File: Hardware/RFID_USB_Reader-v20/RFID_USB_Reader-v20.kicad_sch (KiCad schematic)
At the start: 18 parts, among them J1 USB_C_Receptacle, J3 SMD_1x1mm, J5 Conn_01x08, Q1 MMBT2222A, U3 CH340C

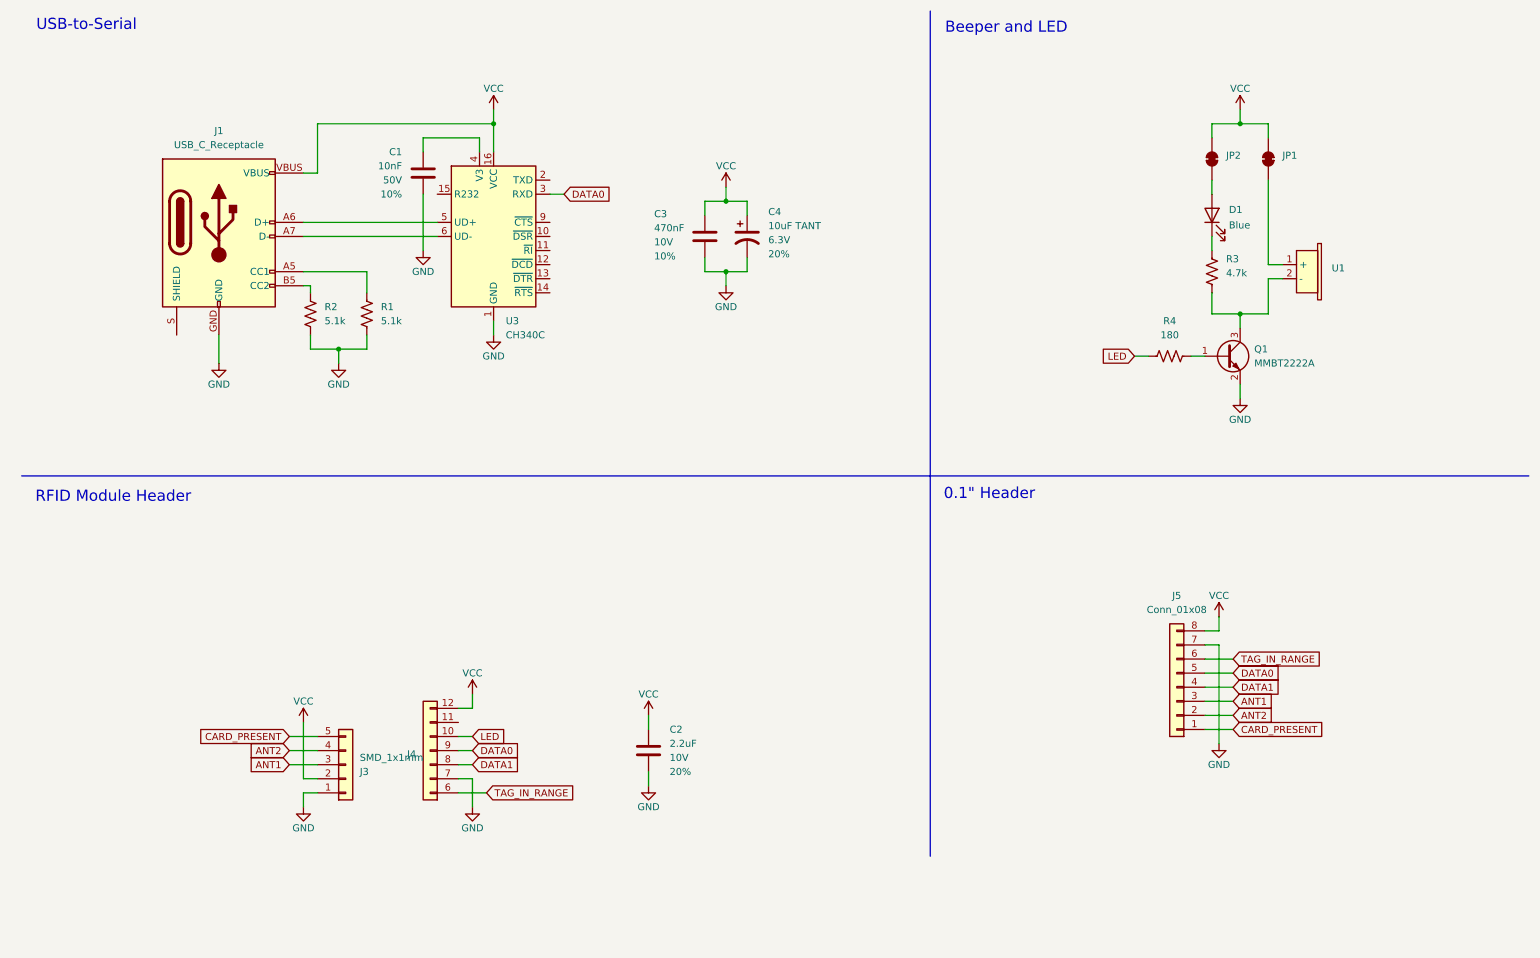
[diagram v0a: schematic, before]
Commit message: Update to small symbols. Add RFID outline device.
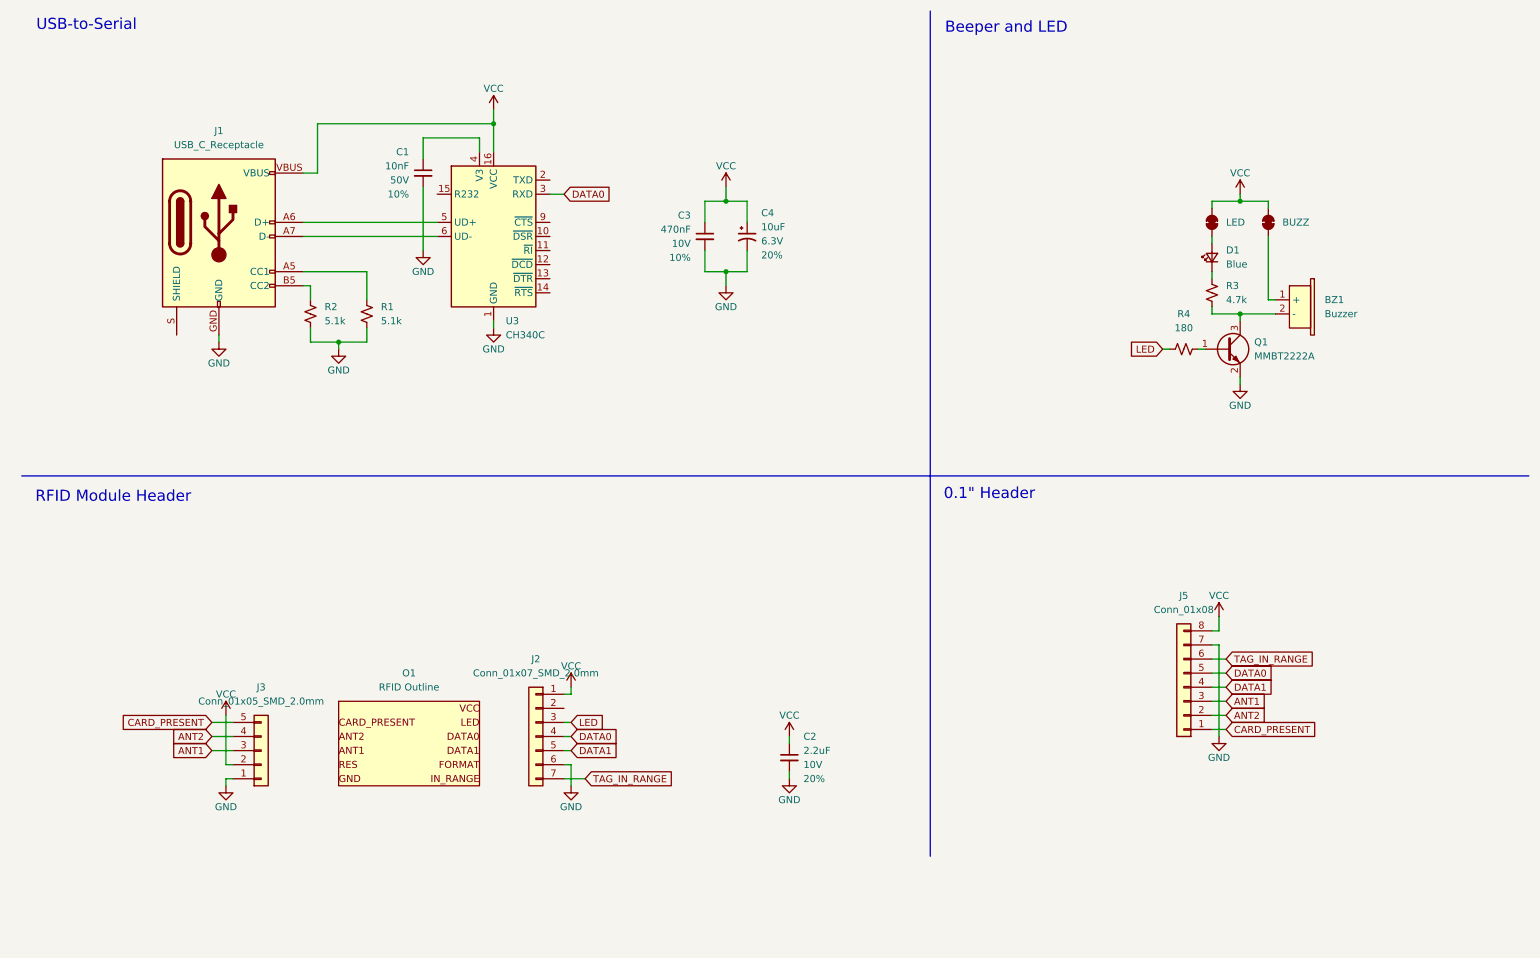
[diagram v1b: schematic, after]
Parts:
- removed J4: ~, SparkFun-Connector:1x07_SMD_2mm, symbol SparkFun-Connector:Conn_01x07_SMD_2mm
- added J2: Conn_01x07_SMD_2.0mm, SparkFun-Connector:1x07_SMD_2mm_Pin1RightDown, symbol SparkFun-Connector:Conn_01x07_SMD_2.0mm_Pin1RightDown
- added O1: RFID Outline, SparkFun-RF:ID-2_12_20_Outline, symbol SparkFun-RF:ID-2/12/20_Outline
- BZ1: renamed from U1; value ~ -> Buzzer; footprint SparkFun-Electromechanical:Buzzer_CCV -> SparkFun-Electromechanical:Buzzer_9mm_SMD; symbol SparkFun-Electromechanical:Buzzer_CCV-084B16 -> SparkFun-Electromechanical:Buzzer_9mm_SMD
- C4: value 10uF TANT -> 10uF; symbol SparkFun-Capacitor:10uF_0603_6.3V_20%_POLAR(TANT) -> SparkFun-Capacitor:10uF_0603_6.3V_20%_Polar(Tant)
- J3: value SMD_1x1mm -> Conn_01x05_SMD_2.0mm; footprint SparkFun-Connector:1x05_SMD_2mm -> SparkFun-Connector:1x05_SMD_2mm_Pin1RightDown; symbol SparkFun-Connector:Conn_01x05_SMD_2mm -> SparkFun-Connector:Conn_01x05_SMD_2.0mm_Pin1RightDown; PROD_ID (none) -> CONN-09344
- JP1: value ~ -> BUZZ
- JP2: value ~ -> LED
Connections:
- net DATA0: now also J2.4 (Pin_4)
- net DATA1: now also J2.5 (Pin_5)
- net GND: now also C4.2, R1.1, R2.1, J2.6 (Pin_6); no longer C4.1, R1.2, R2.2
- net LED: now also R4.1, J2.3 (Pin_3); no longer R4.2
- net TAG_IN_RANGE: now also J2.7 (Pin_7)
- net VCC: now also C4.1, J2.1 (Pin_1); no longer C4.2
- net at Q1.1 (B): now also R4.2; no longer R4.1
- net at BZ1.2 (-), Q1.3 (C): now also R3.1; no longer R3.2
- net at J1.A5 (CC1): now also R1.2; no longer R1.1
- net at J1.B5 (CC2): now also R2.2; no longer R2.1
- net at D1.1 (K): now also R3.2; no longer R3.1
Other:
- moved on the sheet: BZ1, C2, D1, J3, J5, Q1

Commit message: Add fiducials. Add logos. Letter size.
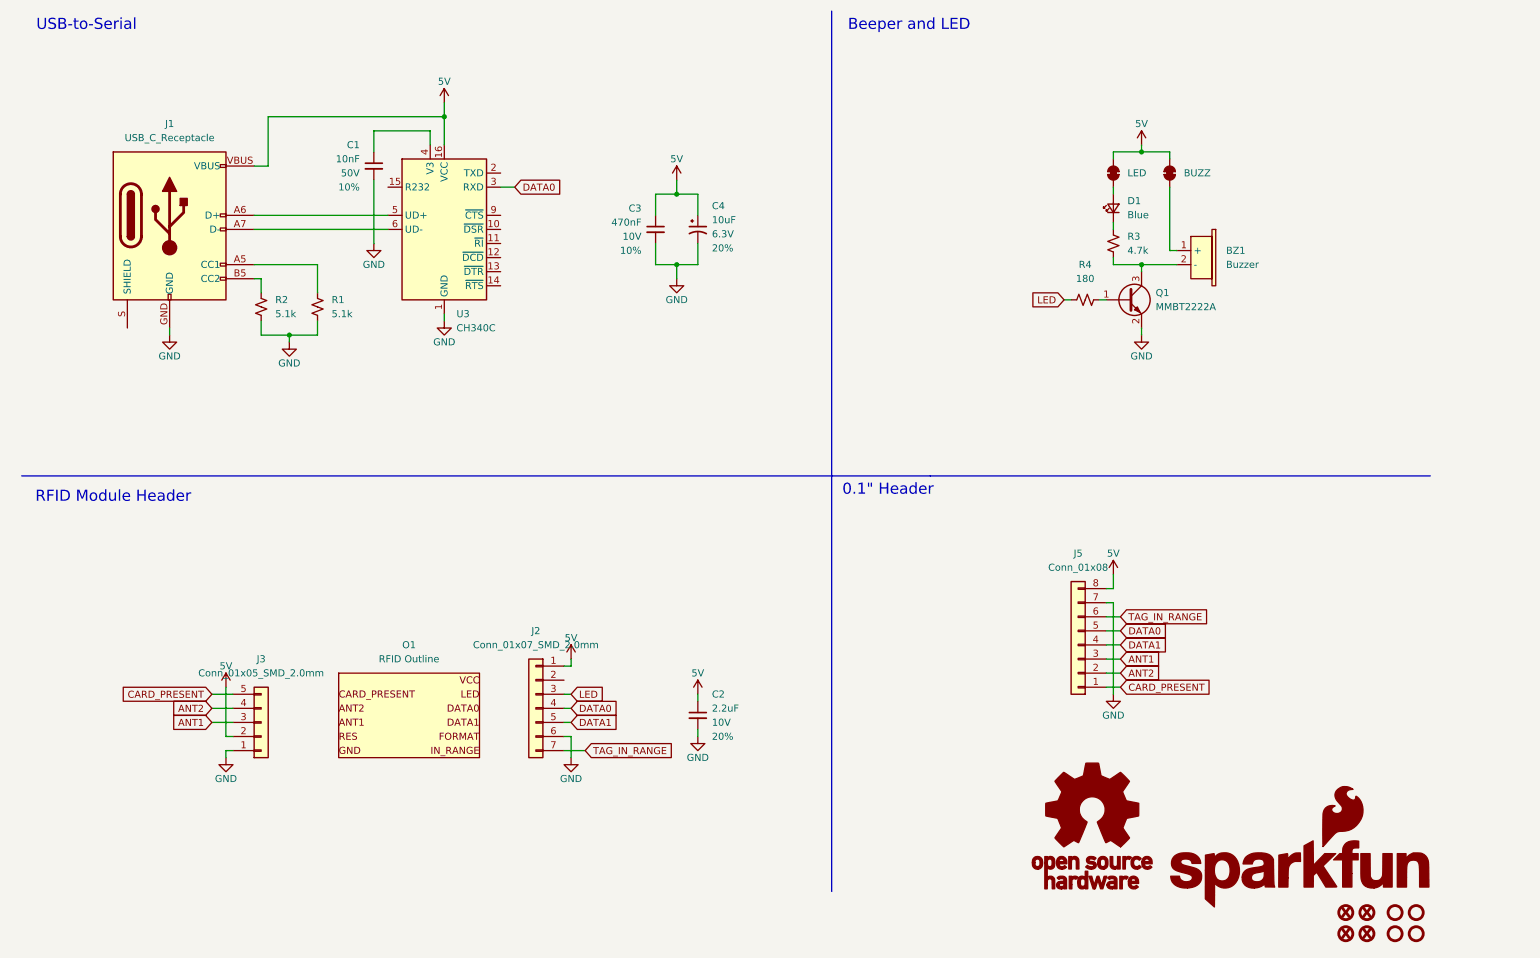
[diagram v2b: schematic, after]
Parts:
- added FID1, FID2, FID3, FID4: Fiducial_0.5mm, SparkFun-Aesthetic:Fiducial_0.5mm_Mask1mm, symbol SparkFun-Aesthetic:Fiducial_0.5mm
- added G1: SparkFun_Logo, symbol SparkFun-Aesthetic:SparkFun_Logo
- added G2: OSHW_Logo, SparkFun-Aesthetic:Creative_Commons_License, symbol SparkFun-Aesthetic:OSHW_Logo
- added ST1, ST2, ST3, ST4: Standoff, SparkFun-Hardware:Standoff, symbol SparkFun-Hardware:Standoff
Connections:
- net VCC renamed 5V
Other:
- company: SparkFun Electronics -> (none)
- moved on the sheet: BZ1, C1, C2, C3, C4, D1, J1, J2, J3, J5, O1, Q1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

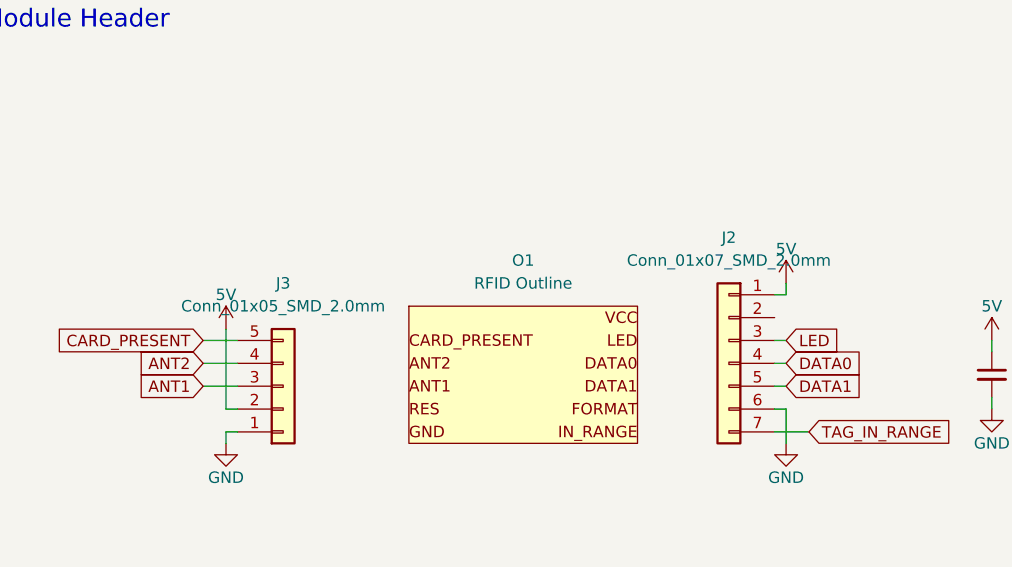
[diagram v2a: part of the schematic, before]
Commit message: Add 3D models
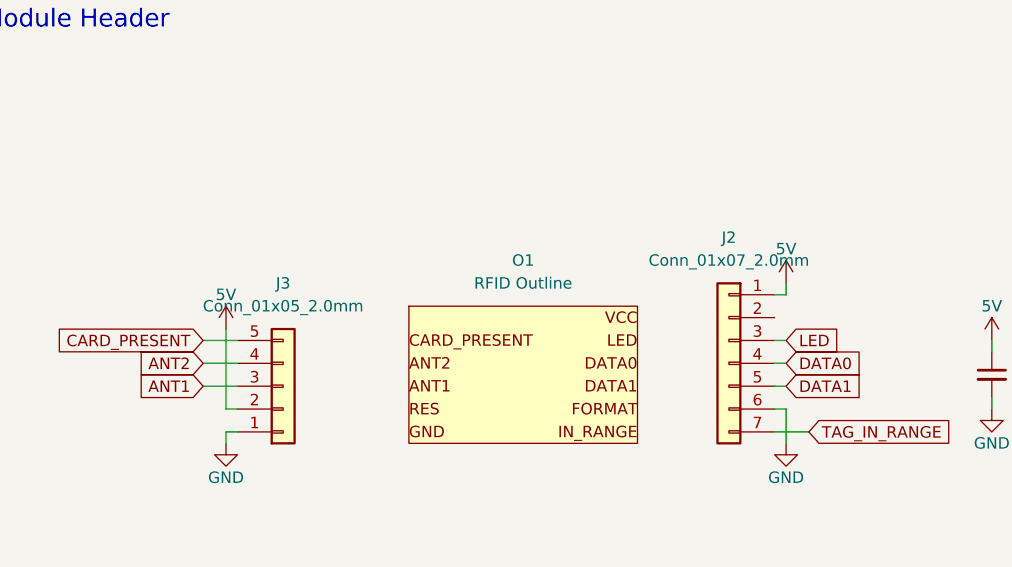
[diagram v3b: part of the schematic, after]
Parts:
- J2: value Conn_01x07_SMD_2.0mm -> Conn_01x07_2.0mm; footprint SparkFun-Connector:1x07_SMD_2mm_Pin1RightDown -> SparkFun-Connector:1x07_2.0mm_SMD_Pin1RightDown; symbol SparkFun-Connector:Conn_01x07_SMD_2.0mm_Pin1RightDown -> SparkFun-Connector:Conn_01x07_2.0mm_SMD_Pin1RightDown
- J3: value Conn_01x05_SMD_2.0mm -> Conn_01x05_2.0mm; footprint SparkFun-Connector:1x05_SMD_2mm_Pin1RightDown -> SparkFun-Connector:1x05_2.0mm_SMD_Pin1RightDown; symbol SparkFun-Connector:Conn_01x05_SMD_2.0mm_Pin1RightDown -> SparkFun-Connector:Conn_01x05_2.0mm_SMD_Pin1RightDown
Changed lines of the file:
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@@
 	)
 	(symbol
-		(lib_id "SparkFun-Connector:Conn_01x05_SMD_2.0mm_Pin1RightDown")
+		(lib_id "SparkFun-Connector:Conn_01x05_2.0mm_SMD_Pin1RightDown")
 		(at 55.88 140.97 0)
 		(mirror x)
@@
 			)
 		)
-		(property "Value" "Conn_01x05_SMD_2.0mm"
+		(property "Value" "Conn_01x05_2.0mm"
 			(at 55.88 132.08 0)
 			(effects
@@
 			)
 		)
-		(property "Footprint" "SparkFun-Connector:1x05_SMD_2mm_Pin1RightDown"
+		(property "Footprint" "SparkFun-Connector:1x05_2.0mm_SMD_Pin1RightDown"
 			(at 55.88 130.81 0)
 			(effects
@@
 	)
 	(symbol
-		(lib_id "SparkFun-Connector:Conn_01x07_SMD_2.0mm_Pin1RightDown")
+		(lib_id "SparkFun-Connector:Conn_01x07_2.0mm_SMD_Pin1RightDown")
 		(at 105.41 138.43 0)
 		(mirror y)
@@
 			)
 		)
-		(property "Value" "Conn_01x07_SMD_2.0mm"
+		(property "Value" "Conn_01x07_2.0mm"
 			(at 105.41 127 0)
 			(effects
@@
 			)
 		)
-		(property "Footprint" "SparkFun-Connector:1x07_SMD_2mm_Pin1RightDown"
+		(property "Footprint" "SparkFun-Connector:1x07_2.0mm_SMD_Pin1RightDown"
 			(at 105.41 153.67 0)
 			(effects
